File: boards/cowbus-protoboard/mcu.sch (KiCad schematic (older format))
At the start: 11 parts, among them P3 SWD, U1 STM32F030C8T6, Y1 8MHz, Y2 32,768kHz

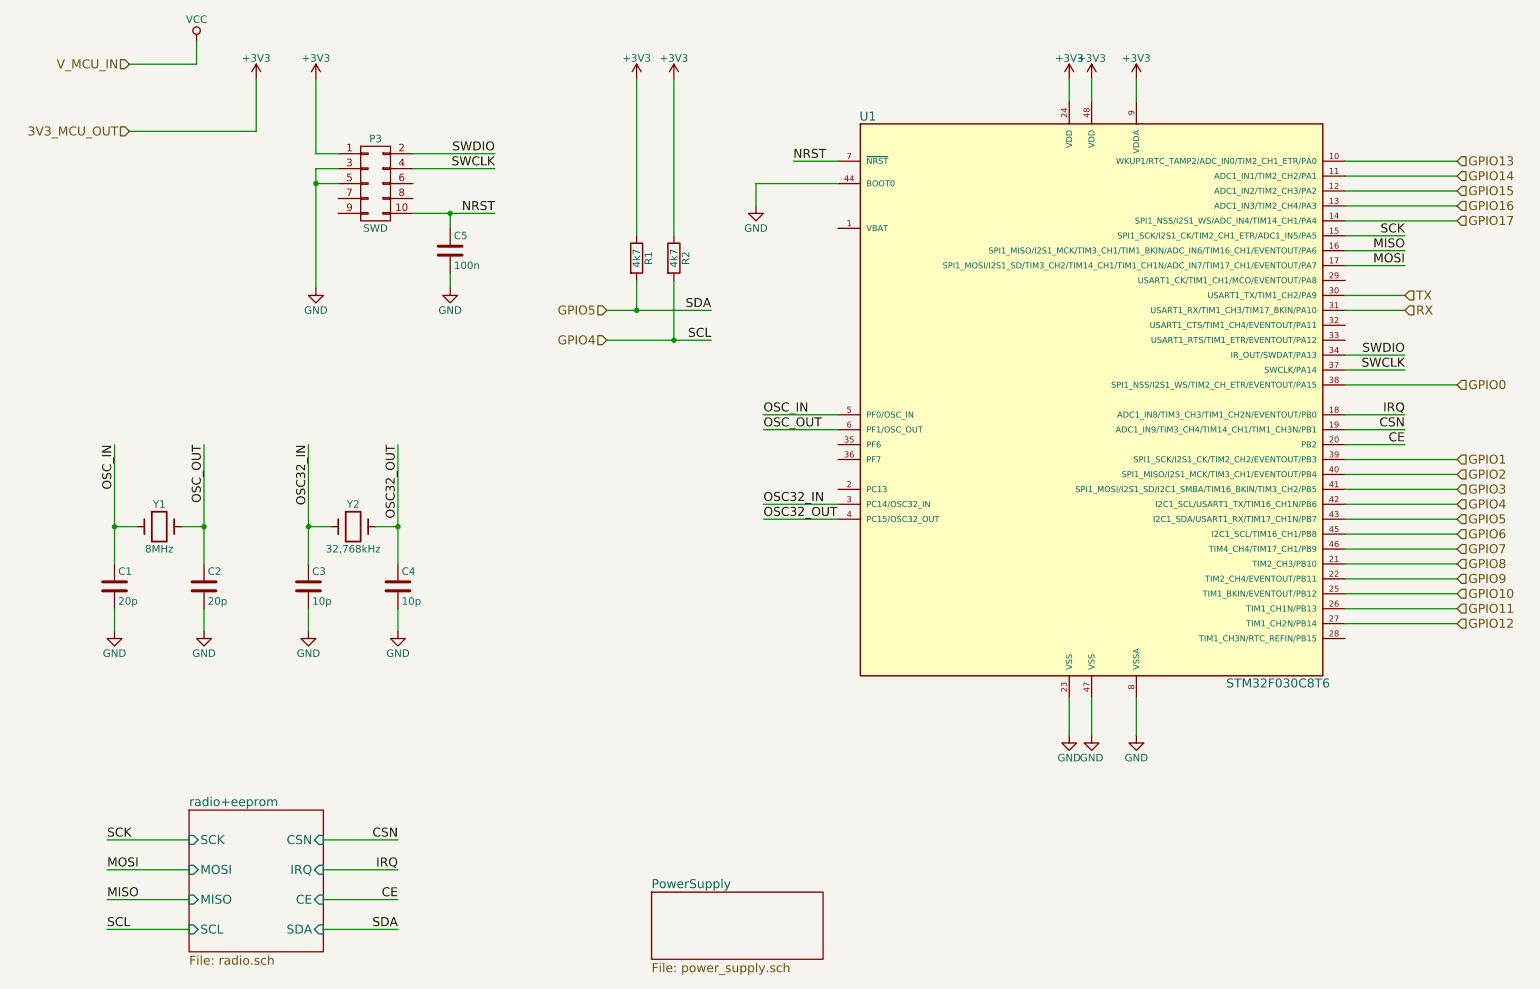
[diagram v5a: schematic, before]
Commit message: added GPIO18, better 3V3, better GND
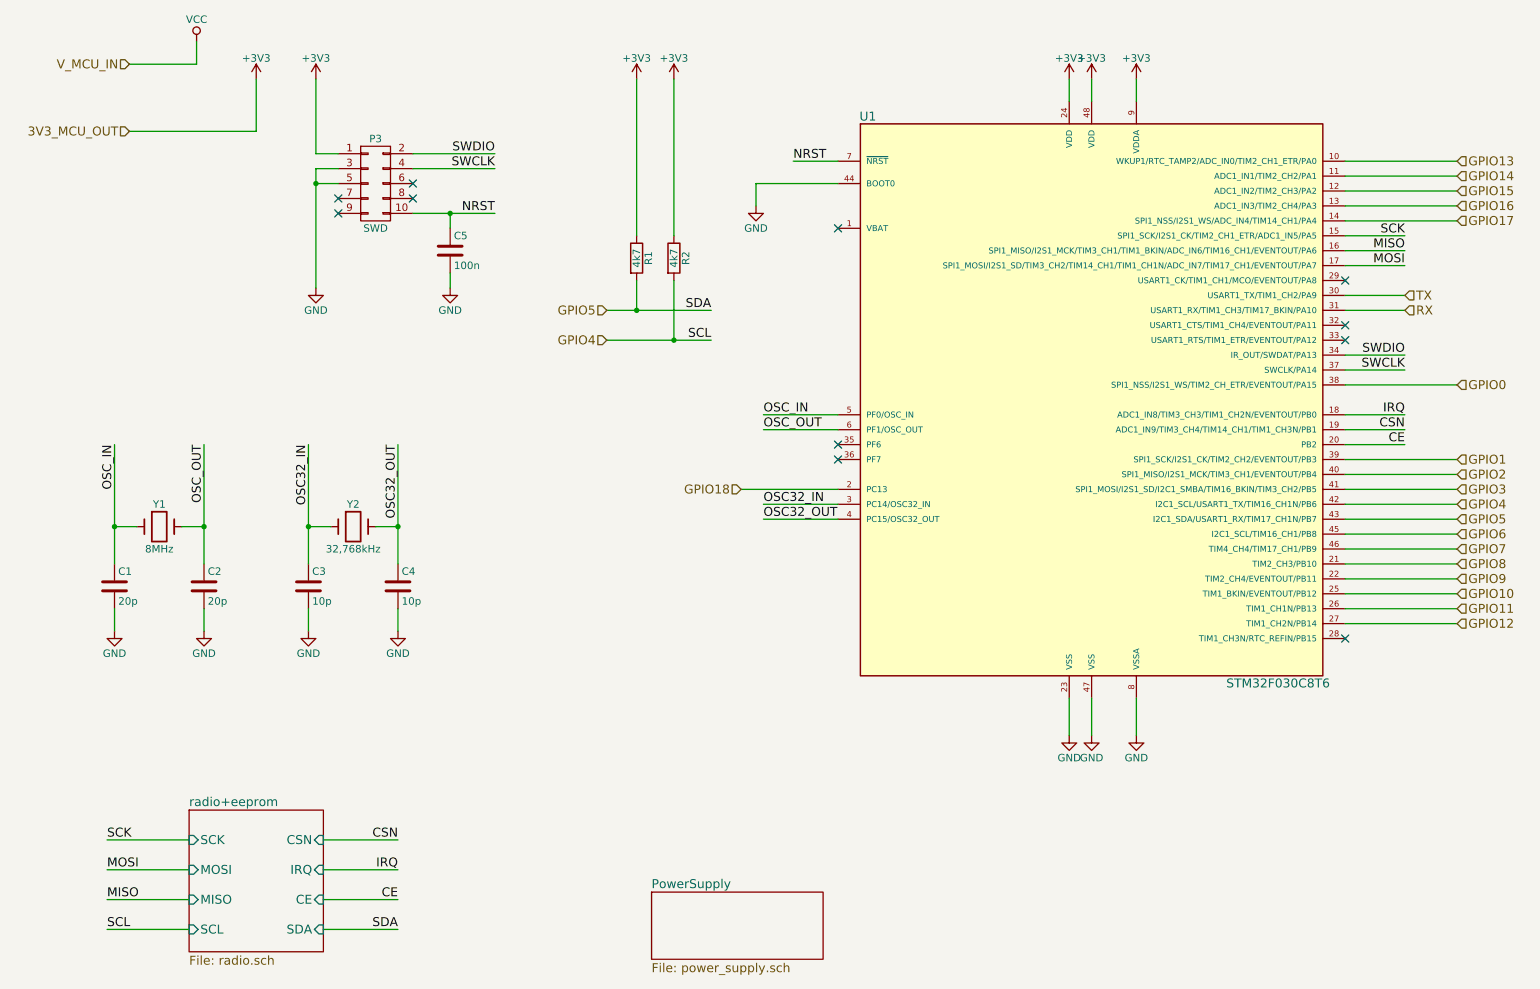
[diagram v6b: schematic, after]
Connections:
- net GPIO18: now reaches U1.2 (PC13)
- no-connect marks 0 -> 11
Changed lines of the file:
@@
 $EndSheet
 $Comp
-L GND #PWR18
+L GND #PWR05
 U 1 1 55A547FE
 P 7600 5550
-F 0 "#PWR18" H 7600 5300 50  0001 C CNN
+F 0 "#PWR05" H 7600 5300 50  0001 C CNN
 F 1 "GND" H 7600 5400 50  0000 C CNN
 F 2 "" H 7600 5550 60  0000 C CNN
@@
 $EndComp
 $Comp
-L GND #PWR20
+L GND #PWR06
 U 1 1 55A54837
 P 7750 5550
-F 0 "#PWR20" H 7750 5300 50  0001 C CNN
+F 0 "#PWR06" H 7750 5300 50  0001 C CNN
 F 1 "GND" H 7750 5400 50  0000 C CNN
 F 2 "" H 7750 5550 60  0000 C CNN
@@
 $EndComp
 $Comp
-L GND #PWR22
+L GND #PWR07
 U 1 1 55A54869
 P 8050 5550
-F 0 "#PWR22" H 8050 5300 50  0001 C CNN
+F 0 "#PWR07" H 8050 5300 50  0001 C CNN
 F 1 "GND" H 8050 5400 50  0000 C CNN
 F 2 "" H 8050 5550 60  0000 C CNN
@@
 $EndComp
 $Comp
-L +3V3 #PWR17
+L +3V3 #PWR08
 U 1 1 55A548DE
 P 7600 1150
-F 0 "#PWR17" H 7600 1000 50  0001 C CNN
+F 0 "#PWR08" H 7600 1000 50  0001 C CNN
 F 1 "+3V3" H 7600 1290 50  0000 C CNN
 F 2 "" H 7600 1150 60  0000 C CNN
@@
 $EndComp
 $Comp
-L +3V3 #PWR19
+L +3V3 #PWR09
 U 1 1 55A54917
 P 7750 1150
-F 0 "#PWR19" H 7750 1000 50  0001 C CNN
+F 0 "#PWR09" H 7750 1000 50  0001 C CNN
 F 1 "+3V3" H 7750 1290 50  0000 C CNN
 F 2 "" H 7750 1150 60  0000 C CNN
@@
 $EndComp
 $Comp
-L +3V3 #PWR21
+L +3V3 #PWR010
 U 1 1 55A54949
 P 8050 1150
-F 0 "#PWR21" H 8050 1000 50  0001 C CNN
+F 0 "#PWR010" H 8050 1000 50  0001 C CNN
 F 1 "+3V3" H 8050 1290 50  0000 C CNN
 F 2 "" H 8050 1150 60  0000 C CNN
@@
 $EndComp
 $Comp
-L +3V3 #PWR10
+L +3V3 #PWR011
 U 1 1 55A57211
 P 2550 1150
-F 0 "#PWR10" H 2550 1000 50  0001 C CNN
+F 0 "#PWR011" H 2550 1000 50  0001 C CNN
 F 1 "+3V3" H 2550 1290 50  0000 C CNN
 F 2 "" H 2550 1150 60  0000 C CNN
@@
 $EndComp
 $Comp
-L GND #PWR11
+L GND #PWR012
 U 1 1 55A5724D
 P 2550 2550
-F 0 "#PWR11" H 2550 2300 50  0001 C CNN
+F 0 "#PWR012" H 2550 2300 50  0001 C CNN
 F 1 "GND" H 2550 2400 50  0000 C CNN
 F 2 "" H 2550 2550 60  0000 C CNN
@@
 $EndComp
 $Comp
-L GND #PWR5
+L GND #PWR013
 U 1 1 55A5CA36
 P 1200 4850
-F 0 "#PWR5" H 1200 4600 50  0001 C CNN
+F 0 "#PWR013" H 1200 4600 50  0001 C CNN
 F 1 "GND" H 1200 4700 50  0000 C CNN
 F 2 "" H 1200 4850 60  0000 C CNN
@@
 $EndComp
 $Comp
-L GND #PWR7
+L GND #PWR014
 U 1 1 55A5CA84
 P 1800 4850
-F 0 "#PWR7" H 1800 4600 50  0001 C CNN
+F 0 "#PWR014" H 1800 4600 50  0001 C CNN
 F 1 "GND" H 1800 4700 50  0000 C CNN
 F 2 "" H 1800 4850 60  0000 C CNN
@@
 $EndComp
 $Comp
-L GND #PWR9
+L GND #PWR015
 U 1 1 55A5D626
 P 2500 4850
-F 0 "#PWR9" H 2500 4600 50  0001 C CNN
+F 0 "#PWR015" H 2500 4600 50  0001 C CNN
 F 1 "GND" H 2500 4700 50  0000 C CNN
 F 2 "" H 2500 4850 60  0000 C CNN
@@
 $EndComp
 $Comp
-L GND #PWR12
+L GND #PWR016
 U 1 1 55A5D62C
 P 3100 4850
-F 0 "#PWR12" H 3100 4600 50  0001 C CNN
+F 0 "#PWR016" H 3100 4600 50  0001 C CNN
 F 1 "GND" H 3100 4700 50  0000 C CNN
 F 2 "" H 3100 4850 60  0000 C CNN
@@
 CE
 $Comp
-L GND #PWR13
+L GND #PWR017
 U 1 1 55A57289
 P 3450 2550
-F 0 "#PWR13" H 3450 2300 50  0001 C CNN
+F 0 "#PWR017" H 3450 2300 50  0001 C CNN
 F 1 "GND" H 3450 2400 50  0000 C CNN
 F 2 "" H 3450 2550 60  0000 C CNN
@@
 $EndComp
 $Comp
-L GND #PWR16
+L GND #PWR018
 U 1 1 55A6DF93
 P 5500 2000
-F 0 "#PWR16" H 5500 1750 50  0001 C CNN
+F 0 "#PWR018" H 5500 1750 50  0001 C CNN
 F 1 "GND" H 5500 1850 50  0000 C CNN
 F 2 "" H 5500 2000 60  0000 C CNN
@@
 Connection ~ 3450 2050
 $Comp
-L VCC #PWR6
+L VCC #PWR019
 U 1 1 55A61A9B
 P 1750 900
-F 0 "#PWR6" H 1750 750 50  0001 C CNN
+F 0 "#PWR019" H 1750 750 50  0001 C CNN
 F 1 "VCC" H 1750 1050 50  0000 C CNN
 F 2 "" H 1750 900 60  0000 C CNN
@@
 $EndComp
 $Comp
-L +3V3 #PWR8
+L +3V3 #PWR020
 U 1 1 55A61AE5
 P 2150 1150
-F 0 "#PWR8" H 2150 1000 50  0001 C CNN
+F 0 "#PWR020" H 2150 1000 50  0001 C CNN
 F 1 "+3V3" H 2150 1290 50  0000 C CNN
 F 2 "" H 2150 1150 60  0000 C CNN
@@
 Connection ~ 4950 2900
 $Comp
-L +3V3 #PWR14
+L +3V3 #PWR021
 U 1 1 55A90A74
 P 4700 1150
-F 0 "#PWR14" H 4700 1000 50  0001 C CNN
+F 0 "#PWR021" H 4700 1000 50  0001 C CNN
 F 1 "+3V3" H 4700 1290 50  0000 C CNN
 F 2 "" H 4700 1150 60  0000 C CNN
@@
 $EndComp
 $Comp
-L +3V3 #PWR15
+L +3V3 #PWR022
 U 1 1 55A90A7A
 P 4950 1150
-F 0 "#PWR15" H 4950 1000 50  0001 C CNN
+F 0 "#PWR022" H 4950 1000 50  0001 C CNN
 F 1 "+3V3" H 4950 1290 50  0000 C CNN
 F 2 "" H 4950 1150 60  0000 C CNN
@@
 Text HLabel 9850 2700 2    60   Input ~ 0
 RX
+Wire Wire Line
+	5400 3900 6050 3900
+Text HLabel 5400 3900 0    60   Input ~ 0
+GPIO18
+NoConn ~ 6050 2150
+NoConn ~ 6050 3600
+NoConn ~ 6050 3700
+NoConn ~ 9450 2800
+NoConn ~ 9450 2900
+NoConn ~ 9450 2500
+NoConn ~ 9450 4900
+NoConn ~ 2700 1950
+NoConn ~ 2700 2050
+NoConn ~ 3200 1850
+NoConn ~ 3200 1950
 $EndSCHEMATC
